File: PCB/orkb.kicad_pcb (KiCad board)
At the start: 2 copper layers, 148.5 x 113.3 mm, 114 parts, among them J1 USB_C_Receptacle_USB2.0, P1 OLED, SW1 MXHS, SW10 MXHS, SW11 MXHS, SW12 MXHS, SW13 MXHS, SW14 MXHS, SW15 MXHS, SW16 MXHS, SW17 MXHS, SW18 MXHS, SW19 MXHS, SW2 MXHS, SW20 MXHS, SW21 MXHS, SW22 MXHS, SW23 MXHS, SW24 MSK12C02, SW25 MSK12C02, SW3 MXHS, SW4 MXHS, SW5 MXHS, SW6 MXHS, SW7 MXHS, SW8 MXHS, SW9 MXHS, U1 ProMicro, U2 SRV05-4, U3 SRV05-4

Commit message: Rows and columns routed
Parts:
- moved D27 0.90 mm to (186.8, 61.0)
- moved D5 0.90 mm to (186.8, 61.0)
- moved LED25 0.52 mm to (174.0, 60.8)
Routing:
- net row3: track 17.0 -> 127.8 mm
- net row2: track 19.8 -> 114.4 mm
- net row1: track 19.8 -> 114.2 mm
- net row0: track 19.8 -> 110.9 mm
- net col0: track 51.2 -> 121.6 mm
- net col3: track 12.0 -> 72.0 mm
- net col1: track 46.0 -> 102.4 mm
- net col2: track 46.6 -> 99.1 mm
- net Net-(D27-A): track 11.0 -> 12.3 mm
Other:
- outline, holes or cut-outs redrawn

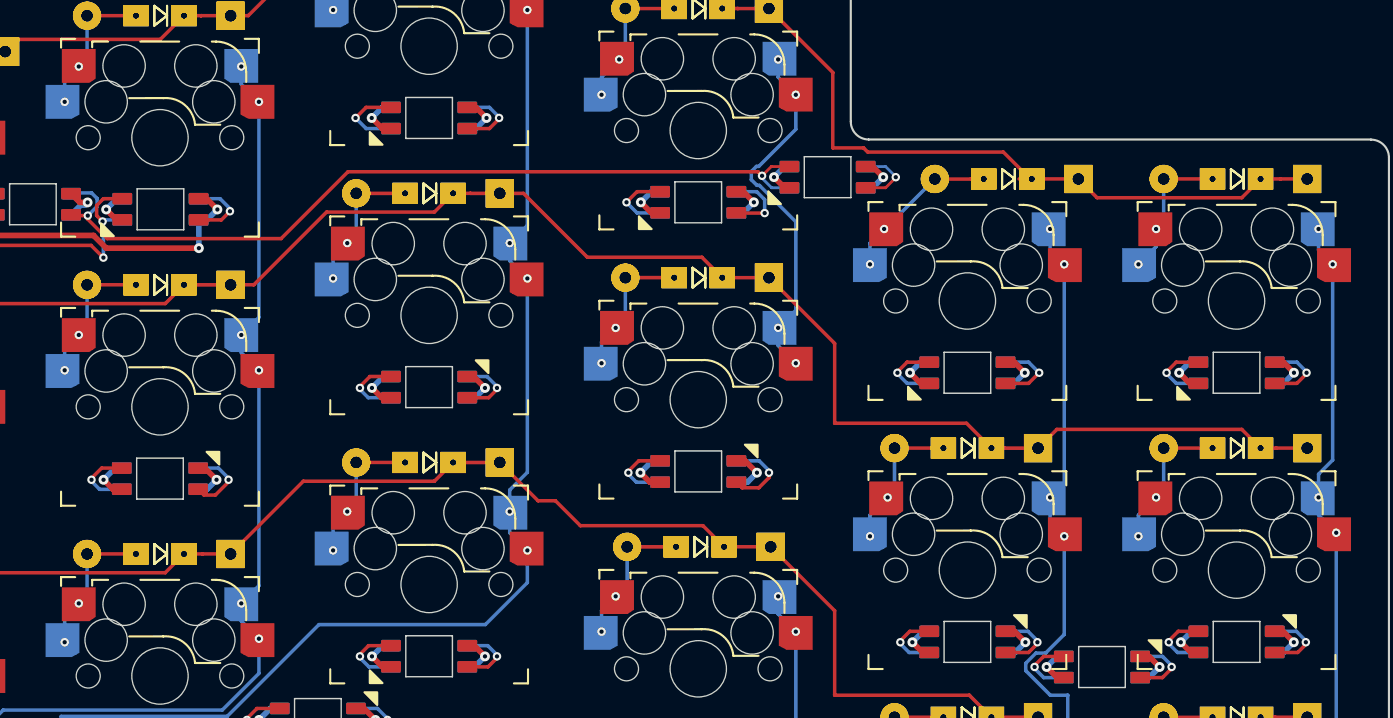
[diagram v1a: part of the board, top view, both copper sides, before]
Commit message: Row0 per key and under-glow RGB routing
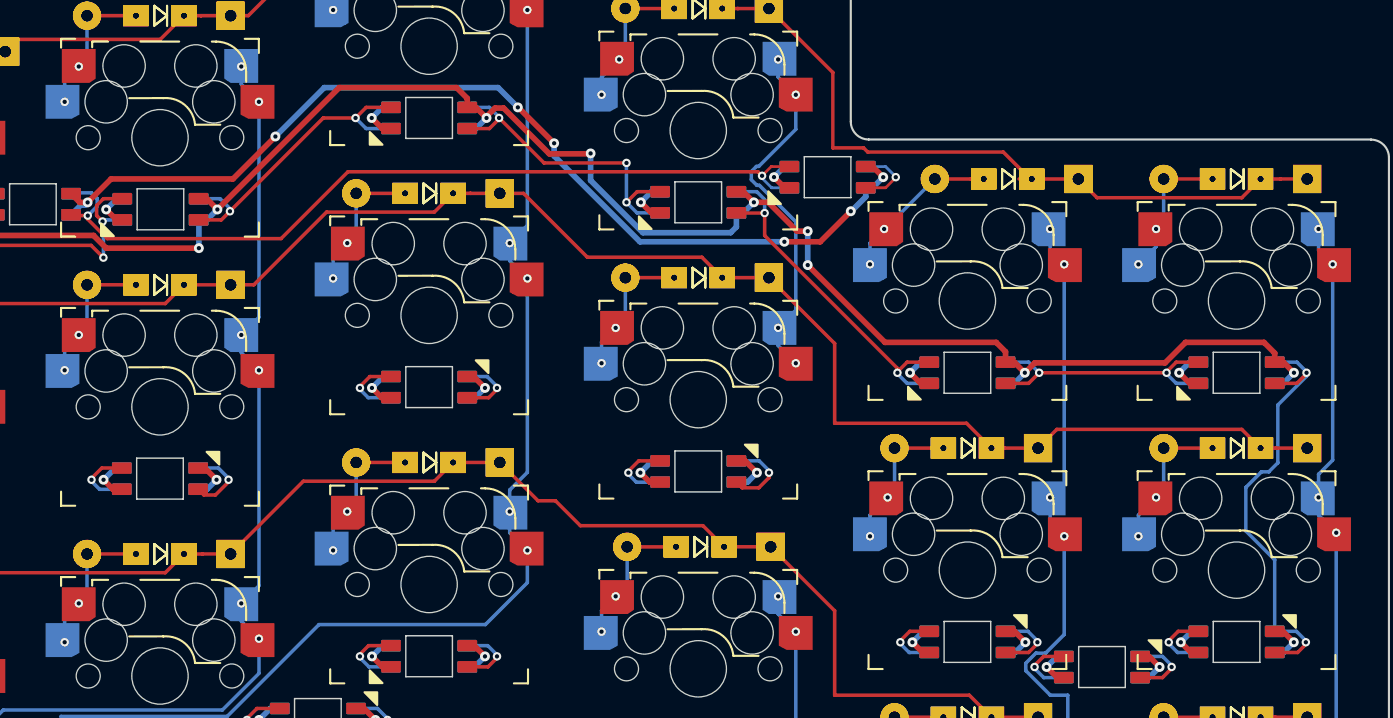
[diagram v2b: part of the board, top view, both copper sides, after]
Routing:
- net /PWR_KEY: track 108.3 -> 198.3 mm, vias 25 -> 28
- net /PWR_GLOW: track 16.1 -> 81.5 mm, vias 5 -> 10
- net Net-(LED12-DIN): track 10.4 -> 31.6 mm
- net Net-(LED4-DOUT): track 10.4 -> 25.6 mm
- net Net-(LED3-DOUT): track 10.6 -> 23.7 mm, vias 2 -> 3
- net Net-(LED2-DOUT): track 10.8 -> 22.4 mm
- net Net-(LED5-DOUT): track 10.6 -> 19.6 mm

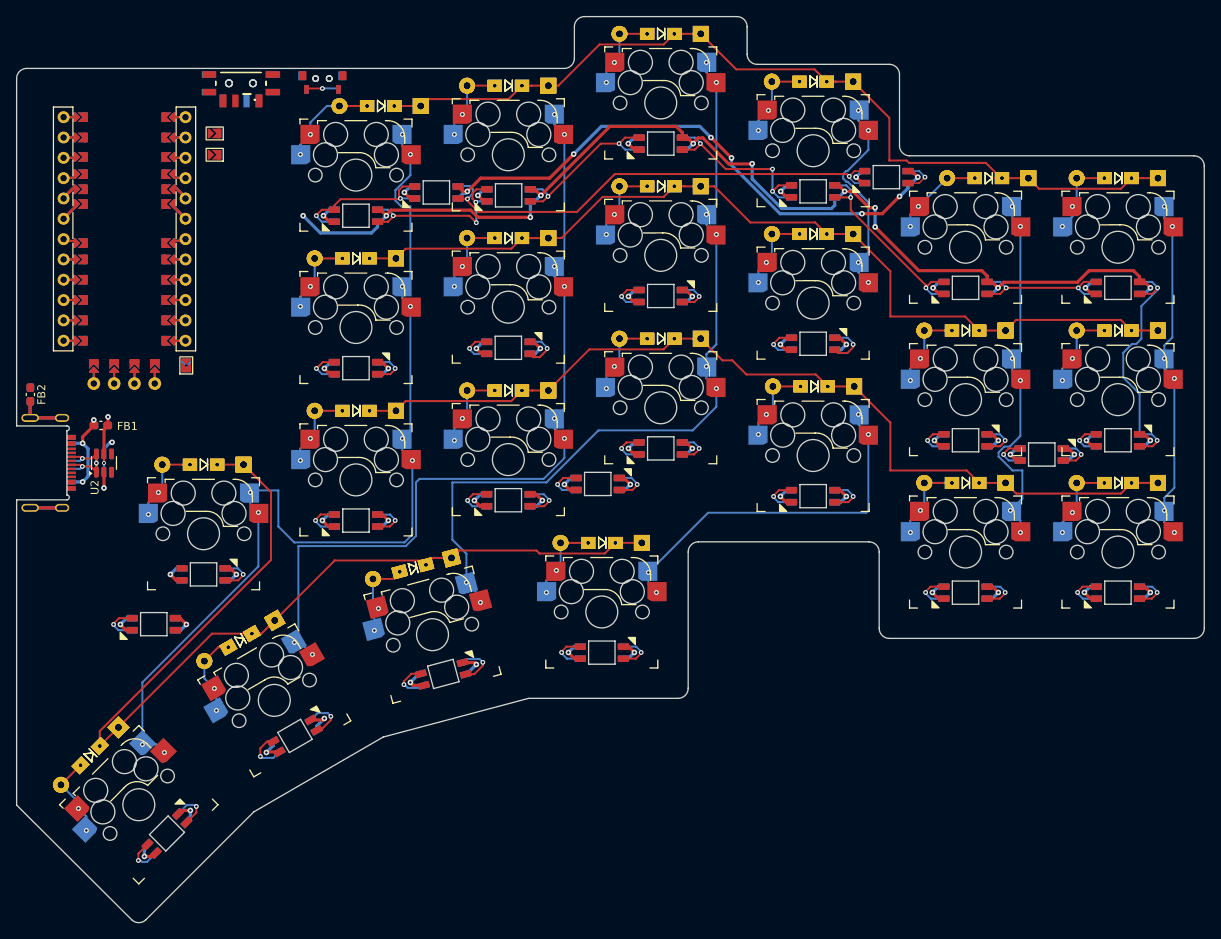
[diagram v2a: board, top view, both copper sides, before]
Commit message: Removing under-glow LEDs (for now)
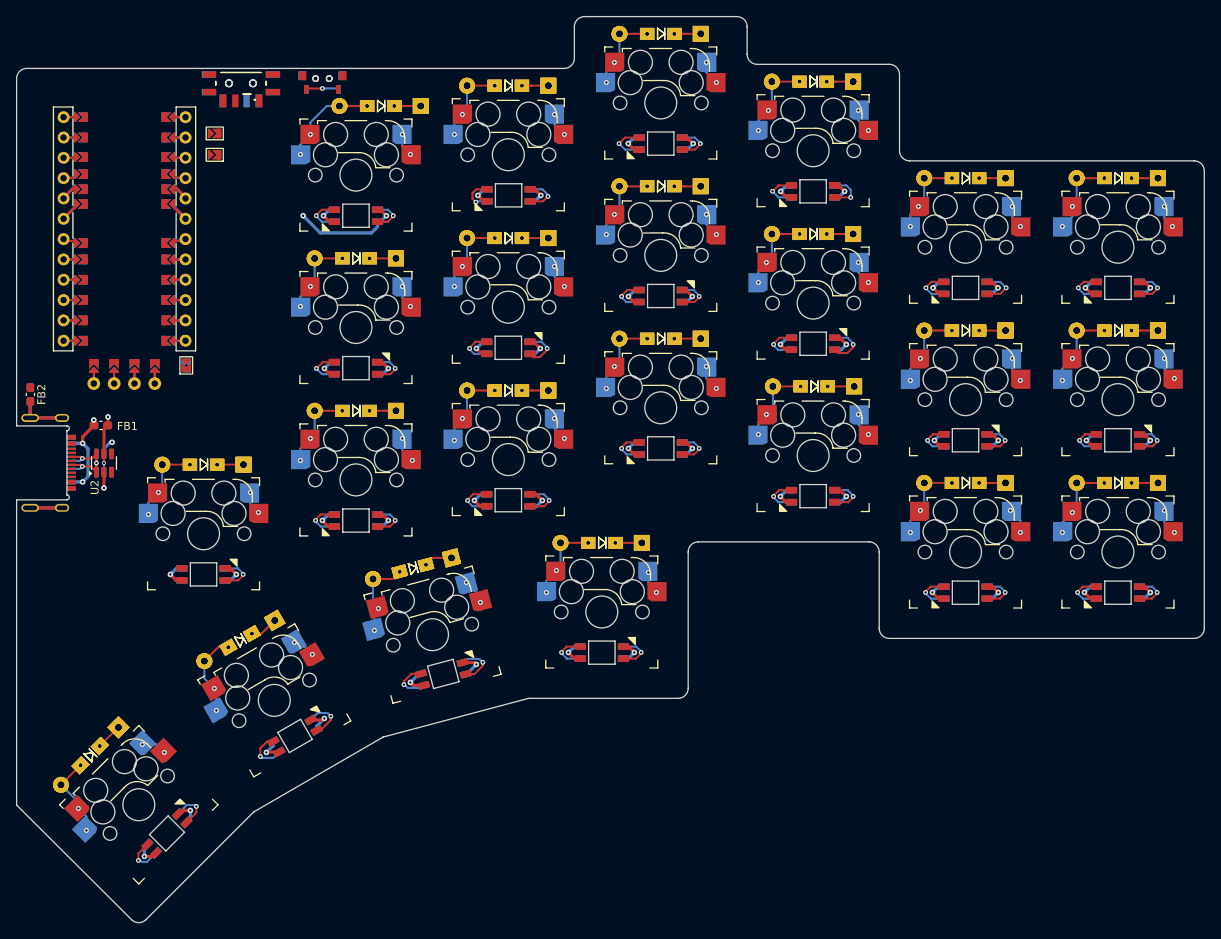
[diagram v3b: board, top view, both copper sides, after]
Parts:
- removed LED24, LED25, LED26, LED27, LED28: SK6803MINI-E, SplitKeyboard_Common:MX_SK6812MINI-E_REVERSIBLE
- moved D27 2.85 mm to (183.9, 61.0)
- moved D5 2.85 mm to (183.9, 61.0)
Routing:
- net row3: track 127.8 -> 17.0 mm
- net /PWR_KEY: track 198.3 -> 87.4 mm, vias 28 -> 24
- net col0: track 121.6 -> 15.2 mm
- net row2: track 114.4 -> 19.8 mm
- net row1: track 114.2 -> 19.8 mm
- net row0: track 110.9 -> 19.8 mm
- net col1: track 102.4 -> 11.9 mm
- net col2: track 99.1 -> 12.5 mm
- net /PWR_GLOW: track 81.5 -> 0.00 mm, vias 10 -> 0
- net Net-(LED24-DOUT): track 60.3 -> 0.00 mm, vias 2 -> 0
- net col3: track 72.0 -> 12.0 mm
- net col4: track 46.6 -> 9.35 mm
- net col5: track 43.1 -> 9.20 mm
- net Net-(LED12-DIN): track 31.6 -> 10.4 mm
- net GND: track 98.7 -> 82.3 mm, vias 30 -> 25
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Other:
- outline, holes or cut-outs redrawn

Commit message: Per key RBG, Switch column and row routing complete
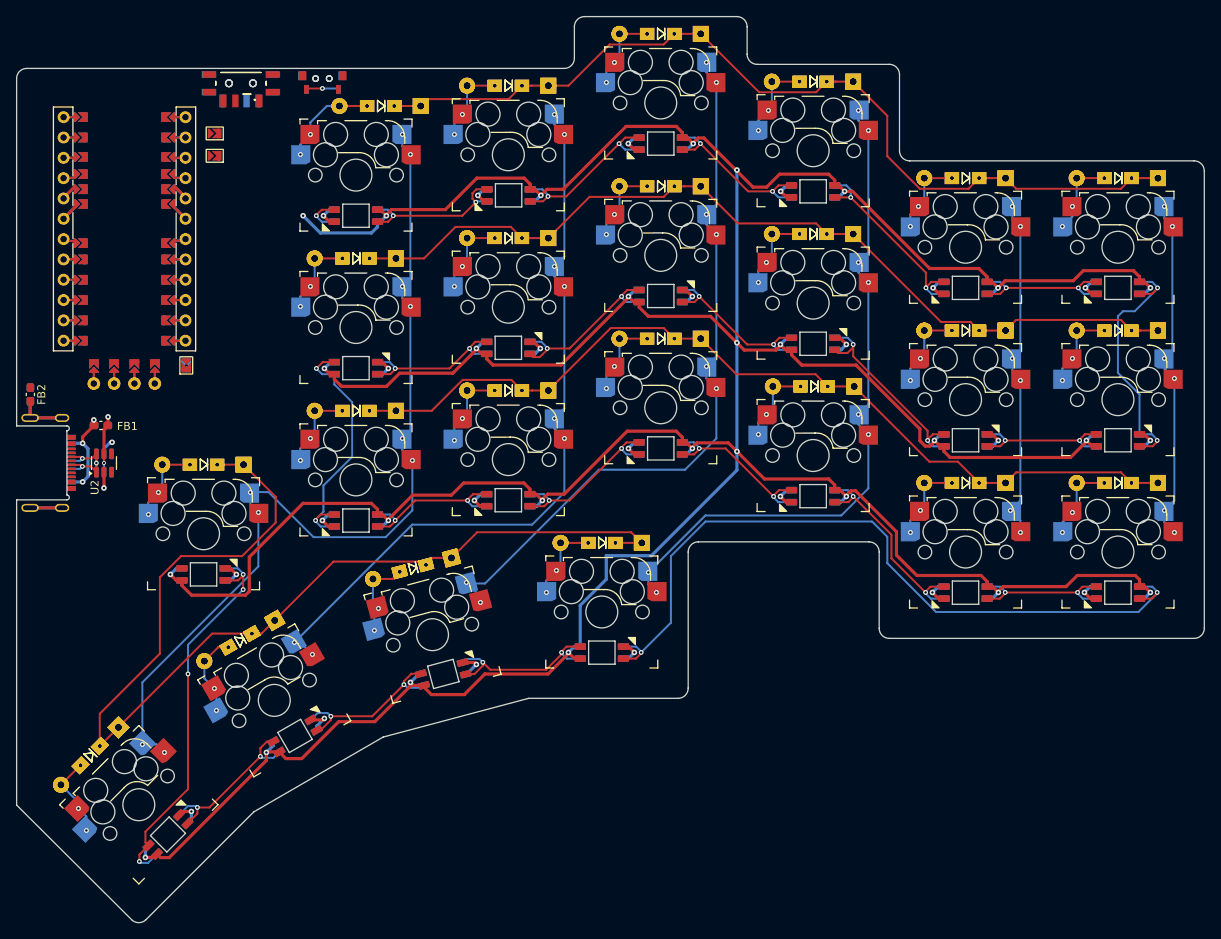
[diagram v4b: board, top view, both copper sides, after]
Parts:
- moved LED20 0.18 mm to (84.2, 143.0)
- moved JP3 0.13 mm to (90.0, 58.2)
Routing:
- net /PWR_KEY: track 87.4 -> 578.5 mm, vias 24 -> 27
- net row3: track 17.0 -> 136.7 mm
- net col0: track 15.2 -> 114.2 mm
- net row2: track 19.8 -> 113.1 mm
- net row0: track 19.8 -> 112.9 mm
- net row1: track 19.8 -> 112.0 mm
- net Net-(LED18-DOUT): track 10.3 -> 94.2 mm
- net col1: track 11.9 -> 94.2 mm
- net col2: track 12.5 -> 91.6 mm
- net col3: track 12.0 -> 84.6 mm
- net Net-(LED19-DIN): track 10.4 -> 49.5 mm, vias 2 -> 4
- net col5: track 9.20 -> 43.1 mm
- net col4: track 9.35 -> 43.0 mm
- net Net-(LED12-DIN): track 10.4 -> 32.7 mm
- net Net-(LED13-DIN): track 10.5 -> 31.7 mm
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
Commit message: Initial complete routing of PCB
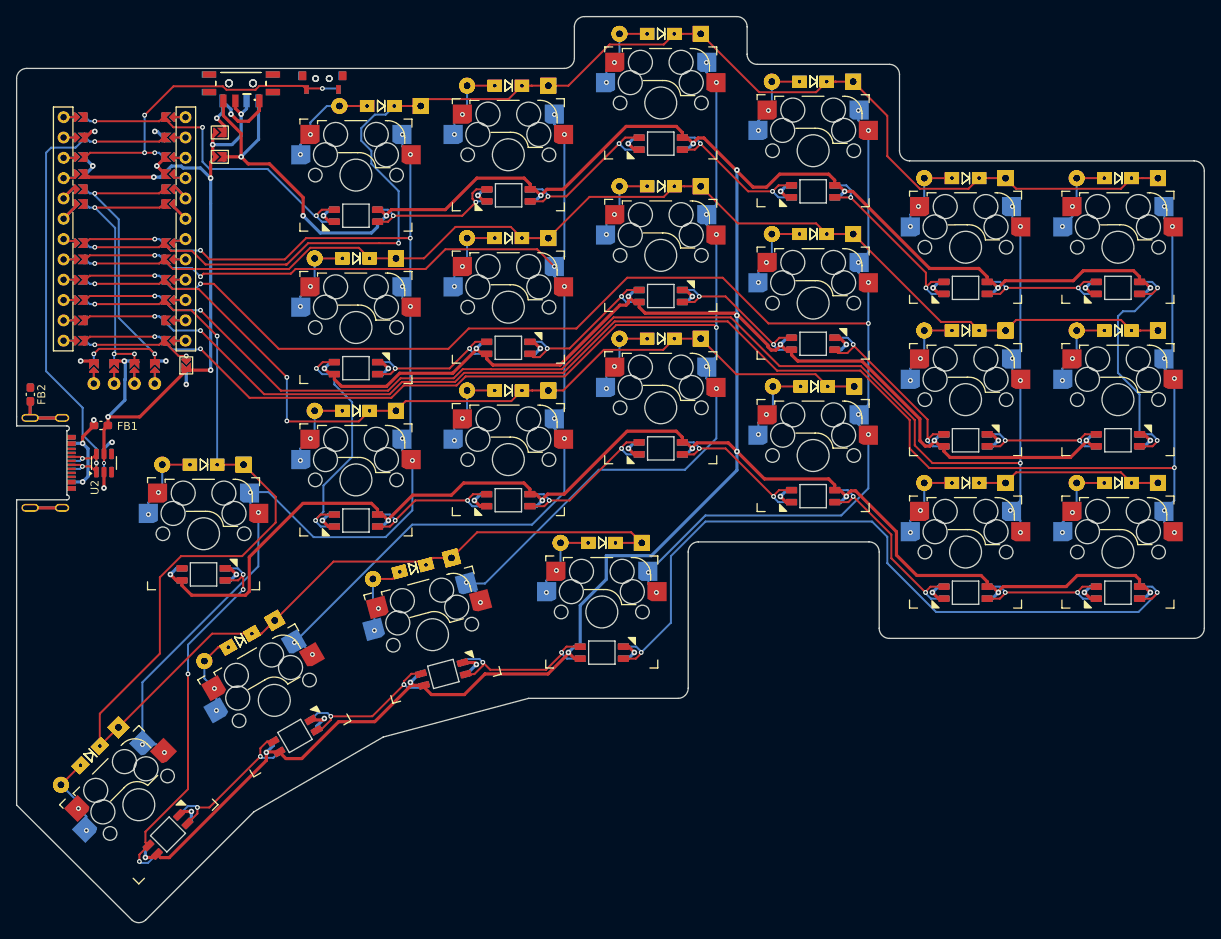
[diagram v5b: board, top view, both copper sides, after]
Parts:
- moved JP3 2.99 mm to (90.7, 55.2)
- moved JP4 2.99 mm to (90.7, 58.3)
- turned JP2 to 90 degrees
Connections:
- JP1 pad 1: Hand -> VCC
- JP1 pad 2: VCC -> Hand
- JP2 pad 1: Hand -> GND
- JP2 pad 2: GND -> Hand
- U1 pad 13: col0 -> col2
- U1 pad 14: col1 -> col5
- U1 pad 15: col2 -> col4
- U1 pad 17: col4 -> col1
- U1 pad 18: col5 -> col0
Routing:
- net col5: track 43.1 -> 196.9 mm, vias 6 -> 9
- net col4: track 43.0 -> 178.2 mm, vias 6 -> 9
- net col3: track 84.6 -> 193.0 mm, vias 8 -> 11
- net col2: track 91.6 -> 177.7 mm, vias 8 -> 11
- net VCC: track 7.11 -> 90.7 mm, vias 2 -> 8
- net row0: track 112.9 -> 176.3 mm, vias 0 -> 2
- net col1: track 94.2 -> 156.4 mm, vias 8 -> 10
- net DATA: track 14.2 -> 70.4 mm, vias 3 -> 4
- net SDA: track 0.00 -> 43.2 mm, vias 0 -> 3
- net col0: track 114.2 -> 157.2 mm, vias 10 -> 13
- net row1: track 112.0 -> 150.1 mm, vias 0 -> 1
- net RESET: track 4.26 -> 41.4 mm, vias 1 -> 4
- net LED: track 5.20 -> 42.1 mm, vias 1 -> 3
- net row3: track 136.7 -> 171.5 mm, vias 0 -> 2
- net SCL: track 0.00 -> 33.8 mm, vias 0 -> 3
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
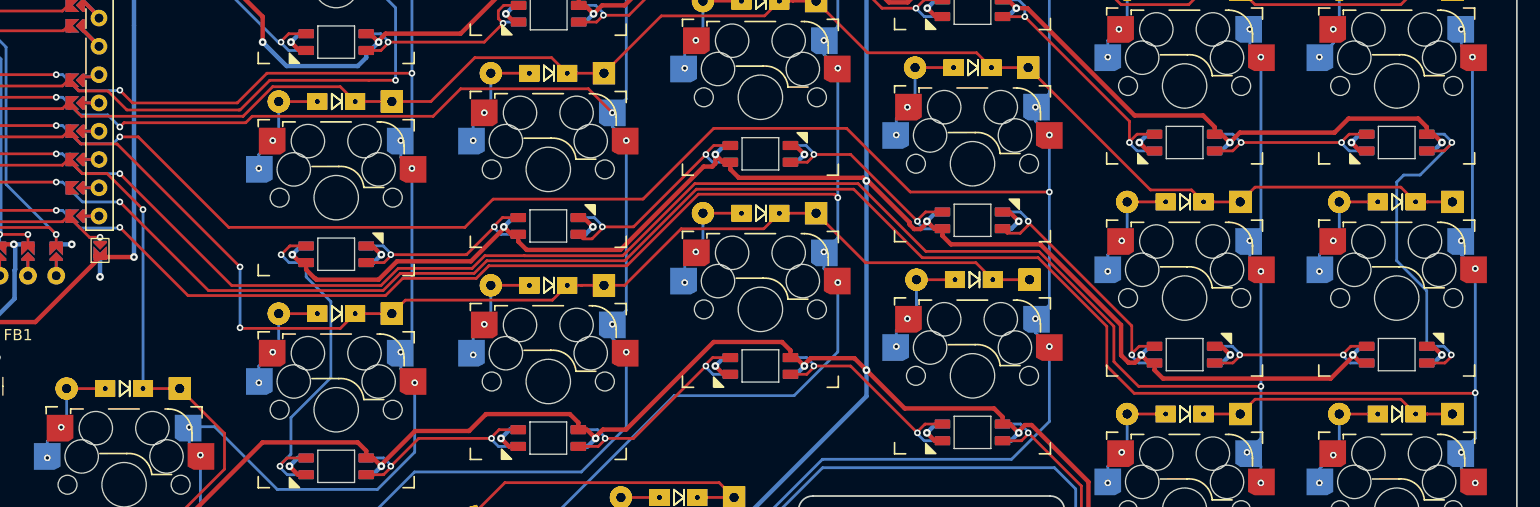
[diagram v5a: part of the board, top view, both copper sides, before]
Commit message: Fixing column order and routing
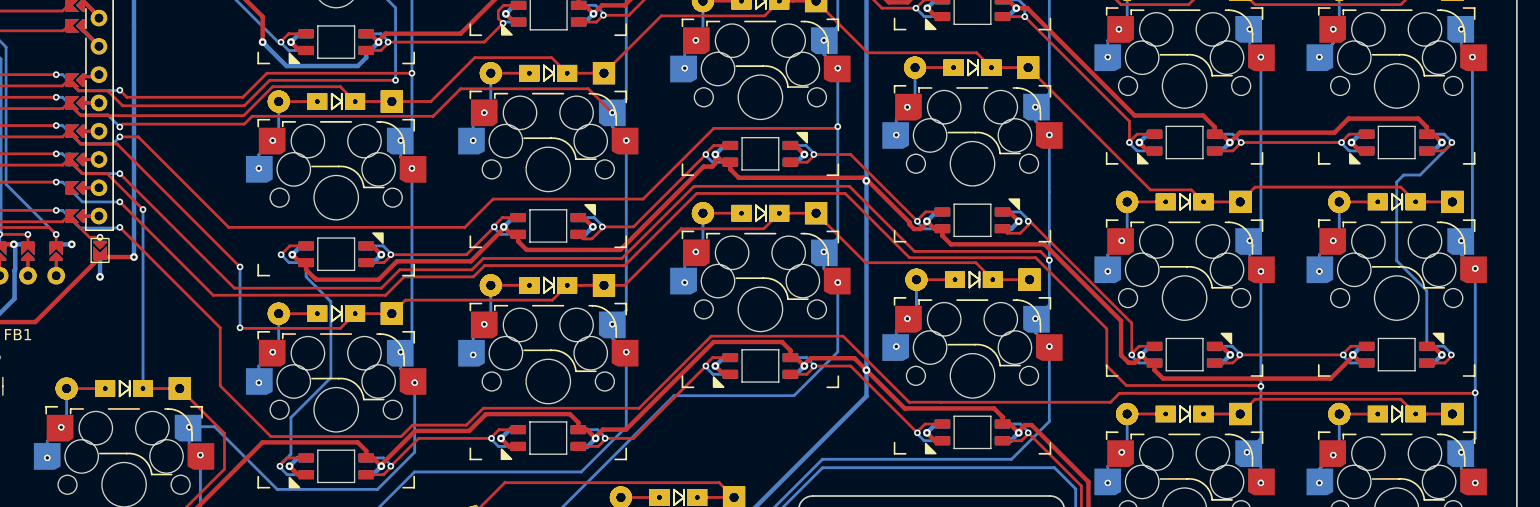
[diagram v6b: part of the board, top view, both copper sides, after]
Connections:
- U1 pad 13: col2 -> col5
- U1 pad 14: col5 -> col4
- U1 pad 15: col4 -> col3
- U1 pad 16: col3 -> col2
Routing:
- net col3: track 193.0 -> 194.2 mm
- net col4: track 178.2 -> 177.2 mm
- net col2: track 177.7 -> 178.7 mm
- net col5: track 196.9 -> 197.5 mm
